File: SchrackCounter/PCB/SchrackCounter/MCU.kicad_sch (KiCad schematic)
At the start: 3 parts, among them U6 ESP32-S3-WROOM-2

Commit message: PCB layout update
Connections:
- net BZ1_PWM: now also U6.12 (IO8)
- net CLK: now also U6.21 (IO13); no longer U6.20 (IO12)
- net GREEN_FLASH: now also U6.23 (IO21)
- net MISO: now also U6.20 (IO12); no longer U6.21 (IO13)
- net MODE: now also U6.39 (IO1)
- net RED_FLASH: now also U6.17 (IO9)
- net RESET: now also U6.35 (IO42)
- net ~{CS1}: now also U6.22 (IO14); no longer U6.17 (IO9)
- net LED_EXT3: now reaches U6.32 (IO39)
- net LED_EXT2: now reaches U6.33 (IO40)
- net LED_EXT1: now reaches U6.34 (IO41)
- net SCHRACK_SW: now reaches U6.38 (IO2)

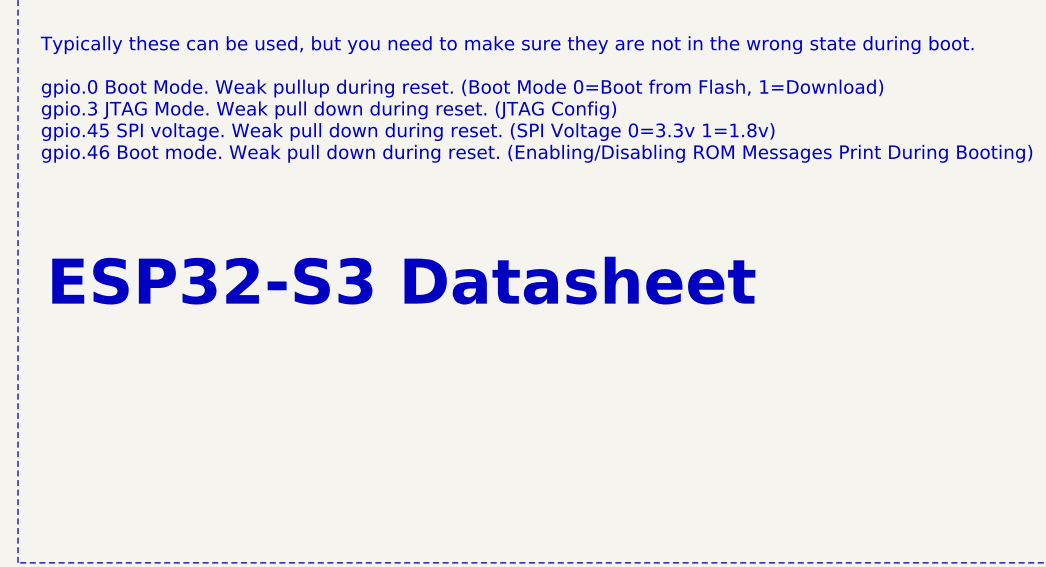
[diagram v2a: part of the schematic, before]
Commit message: PCB update, minor schematic update
PCB routing update, 7segment routing, and minor changes to the 7segments in schematic
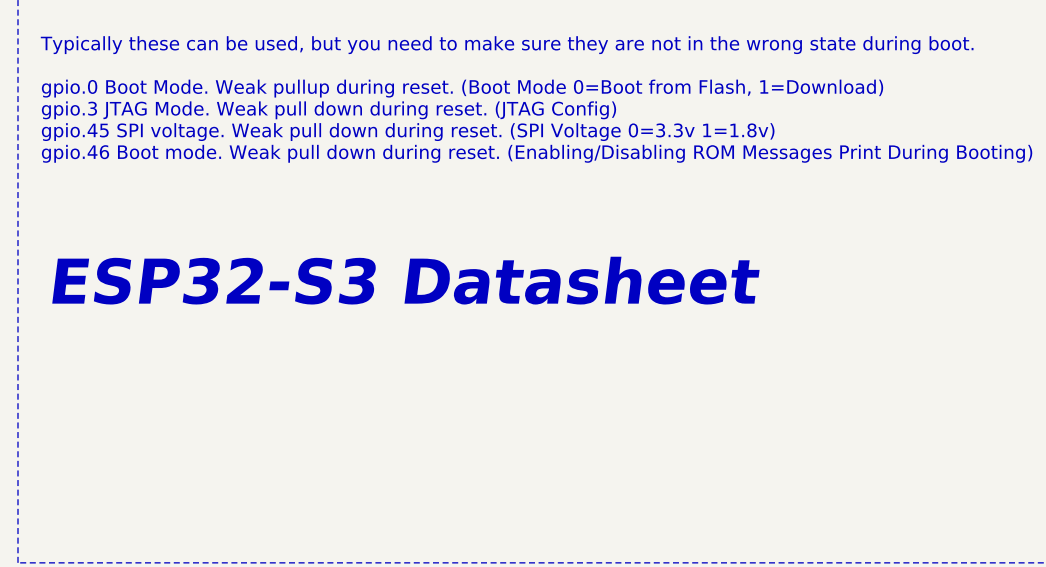
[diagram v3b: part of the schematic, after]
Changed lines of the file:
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@@
 		(effects
 			(font
-				(face "Bahnschrift")
 				(size 5 5)
 				(thickness 1)
 				(bold yes)
-				(color 0 0 0 1)
+				(italic yes)
+				(color 0 0 255 1)
 			)
 			(justify left bottom)

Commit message: SchrackCounter
PCB Finished
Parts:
- C7: value 10uF.mcu -> 10uF
- C8: value 100nF.mcu -> 100nF
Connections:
- net CLK: now also U6.19 (IO11); no longer U6.21 (IO13)
- net GREEN_FLASH: now also U6.17 (IO9); no longer U6.23 (IO21)
- net LED_EXT1: now also U6.32 (IO39); no longer U6.34 (IO41)
- net LED_EXT2: now also U6.31 (IO38); no longer U6.33 (IO40)
- net LED_EXT3: now also U6.23 (IO21); no longer U6.32 (IO39)
- net MISO: now also U6.18 (IO10); no longer U6.20 (IO12)
- net MODE: now also U6.33 (IO40); no longer U6.39 (IO1)
- net MOSI: now also U6.20 (IO12); no longer U6.19 (IO11)
- net RED_FLASH: now also U6.22 (IO14); no longer U6.17 (IO9)
- net SCHRACK_SW: now also U6.34 (IO41); no longer U6.38 (IO2)
- net ~{CS0}: now also U6.4 (IO4); no longer U6.18 (IO10)
- net ~{CS1}: now also U6.21 (IO13); no longer U6.22 (IO14)

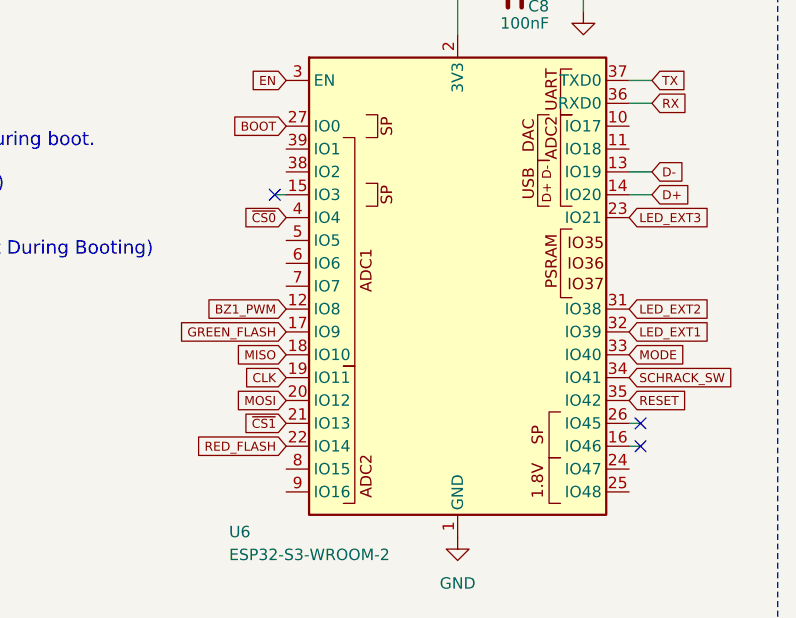
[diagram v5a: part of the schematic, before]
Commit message: PCB LAYOUT UPDATE
Routing, gnd planes
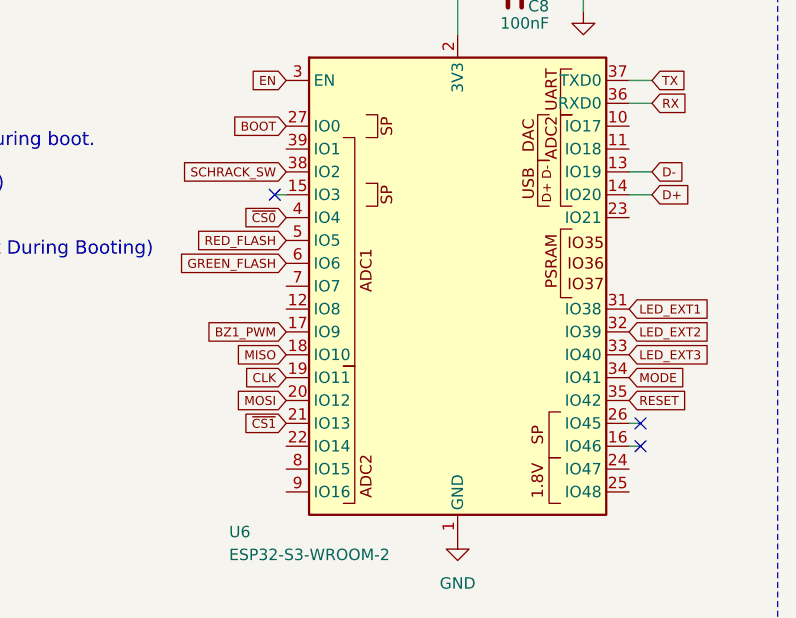
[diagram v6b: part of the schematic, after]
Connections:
- net BZ1_PWM: now also U6.17 (IO9); no longer U6.12 (IO8)
- net GREEN_FLASH: now also U6.6 (IO6); no longer U6.17 (IO9)
- net LED_EXT1: now also U6.31 (IO38); no longer U6.32 (IO39)
- net LED_EXT2: now also U6.32 (IO39); no longer U6.31 (IO38)
- net LED_EXT3: now also U6.33 (IO40); no longer U6.23 (IO21)
- net MODE: now also U6.34 (IO41); no longer U6.33 (IO40)
- net RED_FLASH: now also U6.5 (IO5); no longer U6.22 (IO14)
- net SCHRACK_SW: now also U6.38 (IO2); no longer U6.34 (IO41)

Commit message: PCB finalizing
Final routing and layout
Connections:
- no-connect marks 3 -> 14
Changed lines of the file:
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@@
+	)
+	(no_connect
+		(at 176.53 114.3)
+	)
+	(no_connect
+		(at 176.53 119.38)
+	)
+	(no_connect
+		(at 219.71 119.38)
+	)
+	(no_connect
+		(at 219.71 88.9)
+	)
+	(no_connect
+		(at 219.71 81.28)
+	)
+	(no_connect
+		(at 176.53 81.28)
 	)
 	(no_connect
@@
 		(at 218.44 111.76)
 	)
+	(no_connect
+		(at 219.71 116.84)
+	)
+	(no_connect
+		(at 176.53 116.84)
+	)
+	(no_connect
+		(at 176.53 96.52)
+	)
+	(no_connect
+		(at 219.71 78.74)
+	)
+	(no_connect
+		(at 176.53 99.06)
+	)
 	(wire
 		(pts
@@
 	(wire
 		(pts
+			(xy 217.17 116.84) (xy 219.71 116.84)
+		)
+		(stroke
+			(width 0)
+			(type default)
+		)
+	)
+	(wire
+		(pts
+			(xy 176.53 116.84) (xy 179.07 116.84)
+		)
+		(stroke
+			(width 0)
+			(type default)
+		)
+	)
+	(wire
+		(pts
+			(xy 176.53 99.06) (xy 179.07 99.06)
+		)
+		(stroke
+			(width 0)
+			(type default)
+		)
+	)
+	(wire
+		(pts
 			(xy 219.71 76.2) (xy 217.17 76.2)
 		)
@@
 	(wire
 		(pts
+			(xy 217.17 88.9) (xy 219.71 88.9)
+		)
+		(stroke
+			(width 0)
+			(type default)
+		)
+	)
+	(wire
+		(pts
 			(xy 219.71 86.36) (xy 217.17 86.36)
 		)
@@
 	(wire
 		(pts
+			(xy 176.53 96.52) (xy 179.07 96.52)
+		)
+		(stroke
+			(width 0)
+			(type default)
+		)
+	)
+	(wire
+		(pts
 			(xy 208.28 63.5) (xy 212.09 63.5)
 		)
@@
 	(wire
 		(pts
+			(xy 217.17 78.74) (xy 219.71 78.74)
+		)
+		(stroke
+			(width 0)
+			(type default)
+		)
+	)
+	(wire
+		(pts
 			(xy 212.09 55.88) (xy 212.09 63.5)
 		)
@@
 	(wire
 		(pts
+			(xy 176.53 81.28) (xy 179.07 81.28)
+		)
+		(stroke
+			(width 0)
+			(type default)
+		)
+	)
+	(wire
+		(pts
 			(xy 218.44 111.76) (xy 217.17 111.76)
 		)
@@
 	(wire
 		(pts
+			(xy 176.53 114.3) (xy 179.07 114.3)
+		)
+		(stroke
+			(width 0)
+			(type default)
+		)
+	)
+	(wire
+		(pts
+			(xy 217.17 119.38) (xy 219.71 119.38)
+		)
+		(stroke
+			(width 0)
+			(type default)
+		)
+	)
+	(wire
+		(pts
 			(xy 198.12 55.88) (xy 198.12 63.5)
 		)
@@
 	(wire
 		(pts
+			(xy 217.17 81.28) (xy 219.71 81.28)
+		)
+		(stroke
+			(width 0)
+			(type default)
+		)
+	)
+	(wire
+		(pts
 			(xy 198.12 63.5) (xy 198.12 68.58)
 		)
 		(stroke
+			(width 0)
+			(type default)
+		)
+	)
+	(wire
+		(pts
+			(xy 176.53 119.38) (xy 179.07 119.38)
+		)
+		(stroke

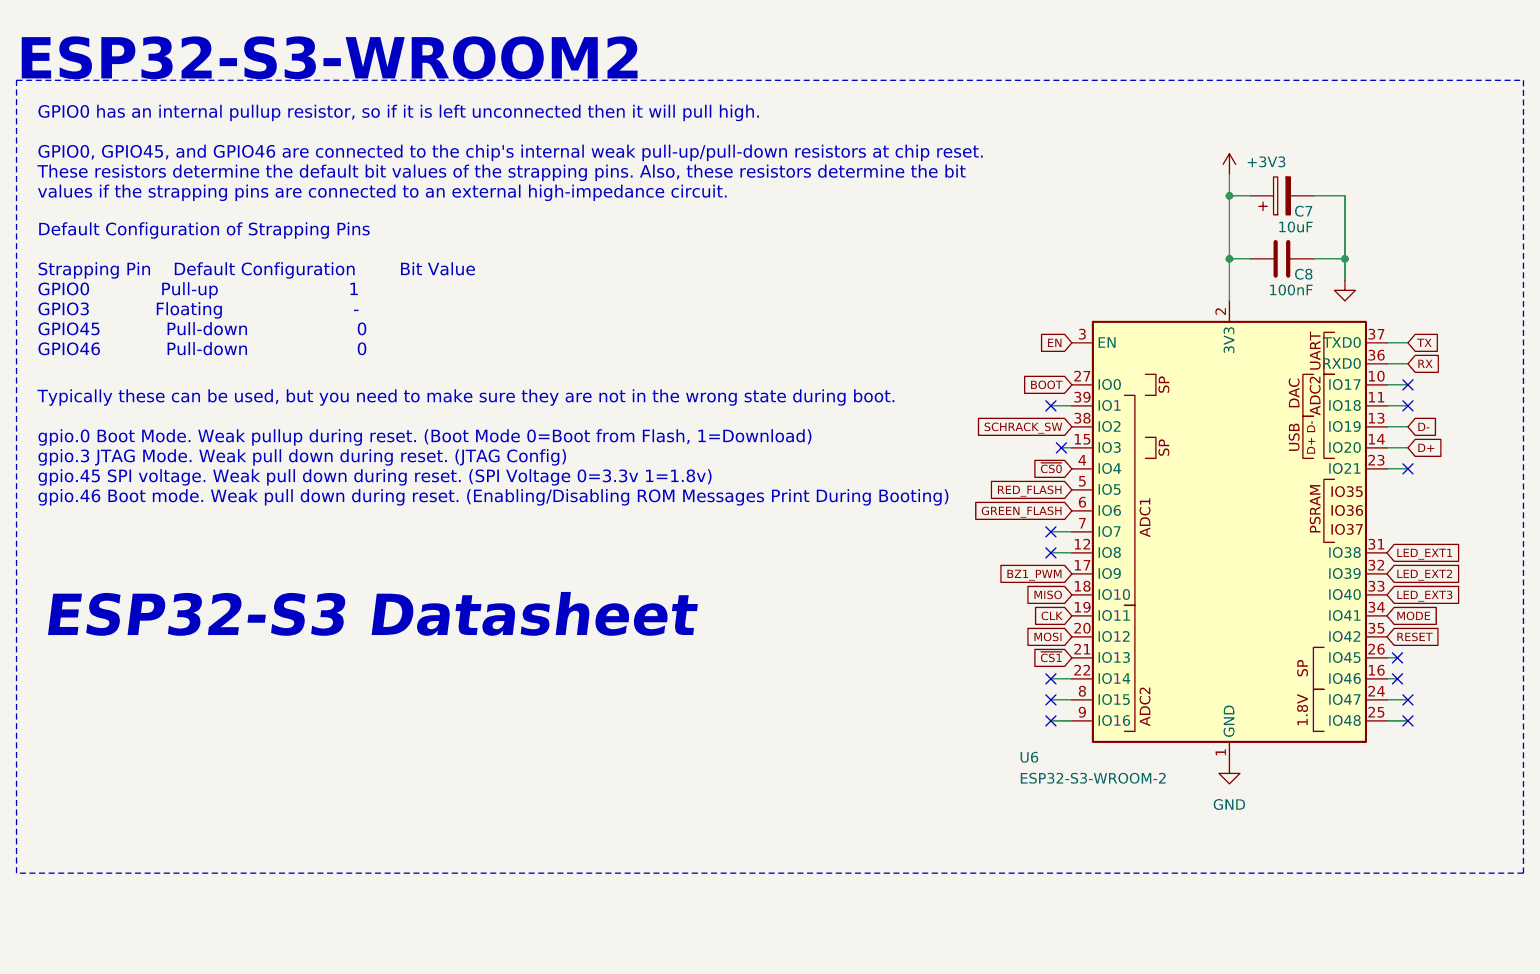
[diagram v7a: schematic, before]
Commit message: Schematic update
Documentation for programming, GPIO pin table :3
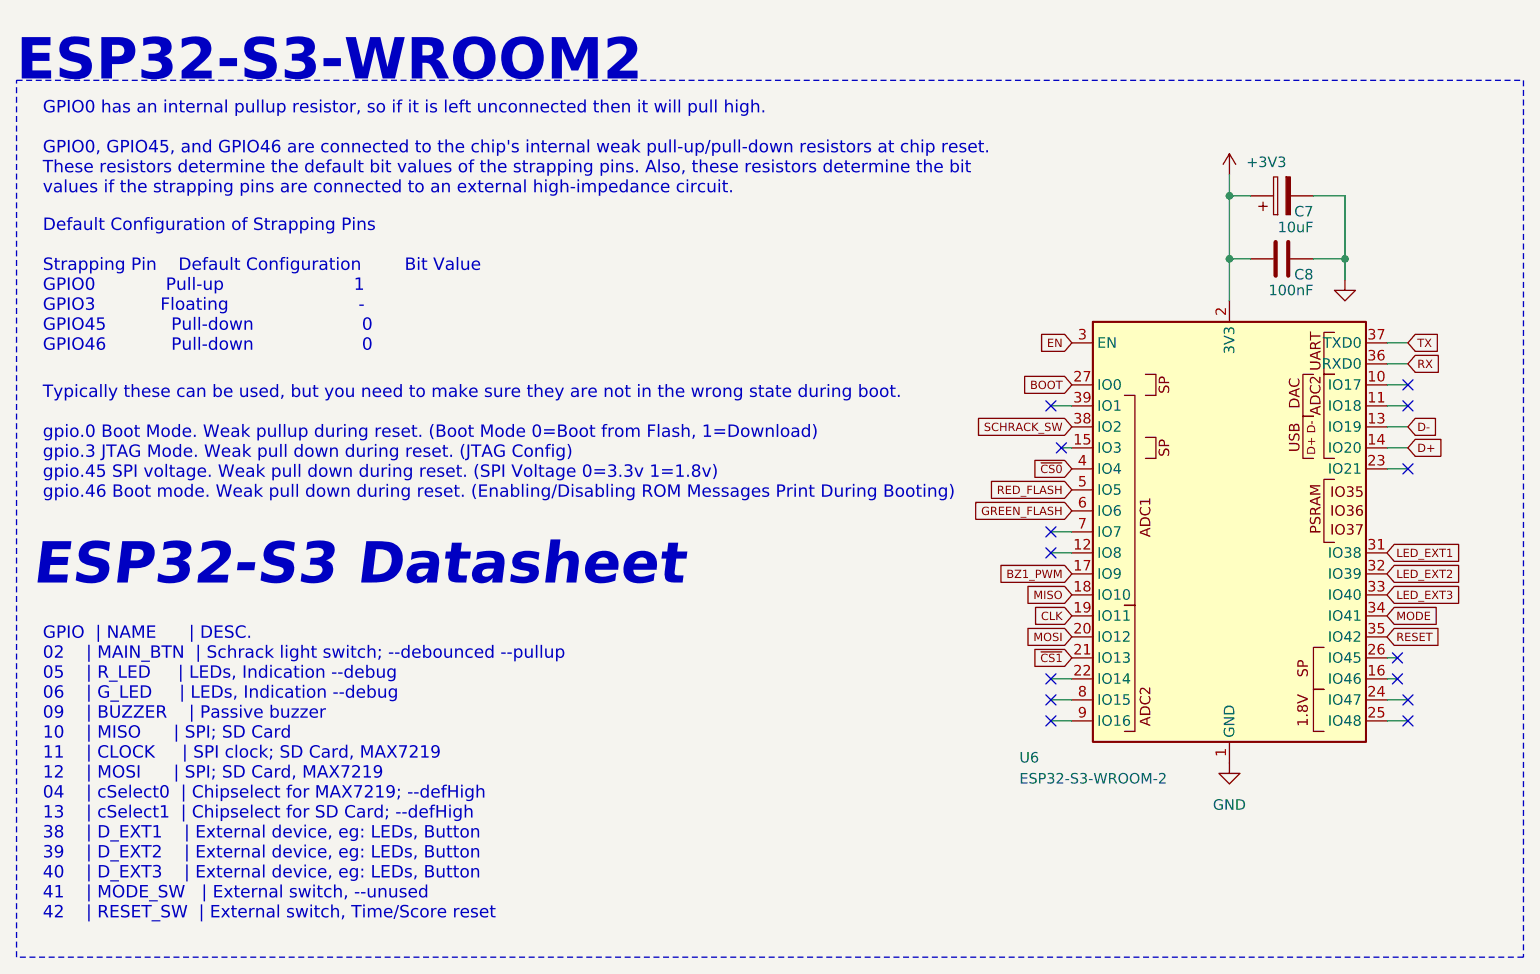
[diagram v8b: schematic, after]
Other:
- note added: "GPIO | NAME | DESC. 02 | MAIN_BTN | Schrack light switch; --debounced --pullup 05 | R_LED | LEDs, Indication --debug 06 | G_LED | LEDs, Indication --debug 09 | BUZZER | Passive buzzer 10 | MISO | SPI; SD Card 11 | CLOCK | SPI clock; SD Card, MAX7219 12 | MOSI | SPI; SD Card, MAX7219 04 | cSelect0 | Chipselect for MAX7219; --defHigh 13 | cSelect1 | Chipselect for SD Card; --defHigh 38 | D_EXT1 | E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"
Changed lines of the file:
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@@
 	(rectangle
 		(start 51.435 41.91)
-		(end 233.68 137.795)
+		(end 233.68 147.955)
 		(stroke
 			(width 0)
@@
 	(text "Default Configuration of Strapping Pins\n\nStrapping Pin	Default Configuration		Bit Value\nGPIO0 			Pull-up						1\nGPIO3			Floating						-\nGPIO45			Pull-down					0\nGPIO46			Pull-down					0"
 		(exclude_from_sim no)
-		(at 53.975 75.565 0)
+		(at 54.61 74.93 0)
 		(effects
 			(font
@@
 			)
 			(justify left bottom)
+		)
+	)
+	(text "GPIO  | NAME      | DESC. \n02    | MAIN_BTN  | Schrack light switch; --debounced --pullup \n05    | R_LED     | LEDs, Indication --debug\n06    | G_LED     | LEDs, Indication --debug\n09    | BUZZER    | Passive buzzer\n10    | MISO      | SPI; SD Card\n11    | CLOCK     | SPI clock; SD Card, MAX7219\n12    | MOSI      | SPI; SD Card, MAX7219\n04    | cSelect0  | Chipselect for MAX7219; --defHigh\n13    | cSelect1  | Chipselect for SD Card; --defHigh\n38    | D_EXT1    | External device, eg: LEDs, Button\n39    | D_EXT2    | External device, eg: LEDs, Button\n40    | D_EXT3    | External device, eg: LEDs, Button\n41    | MODE_SW   | External switch, --unused\n42    | RESET_SW  | External switch, Time/Score reset\n\n"
+		(exclude_from_sim no)
+		(at 54.61 127 0)
+		(effects
+			(font
+				(face "Consolas")
+				(size 1.5 1.5)
+				(color 0 0 0 1)
+			)
+			(justify left)
 		)
 	)
@@
 	(text "GPIO0 has an internal pullup resistor, so if it is left unconnected then it will pull high.\n\nGPIO0, GPIO45, and GPIO46 are connected to the chip's internal weak pull-up/pull-down resistors at chip reset.\nThese resistors determine the default bit values of the strapping pins. Also, these resistors determine the bit\nvalues if the strapping pins are connected to an external high-impedance circuit."
 		(exclude_from_sim no)
-		(at 53.975 56.515 0)
+		(at 54.61 55.88 0)
 		(effects
 			(font
@@
 	(text "Typically these can be used, but you need to make sure they are not in the wrong state during boot.\n\ngpio.0 Boot Mode. Weak pullup during reset. (Boot Mode 0=Boot from Flash, 1=Download)\ngpio.3 JTAG Mode. Weak pull down during reset. (JTAG Config)\ngpio.45 SPI voltage. Weak pull down during reset. (SPI Voltage 0=3.3v 1=1.8v)\ngpio.46 Boot mode. Weak pull down during reset. (Enabling/Disabling ROM Messages Print During Booting)"
 		(exclude_from_sim no)
-		(at 53.975 93.345 0)
+		(at 54.61 92.71 0)
 		(effects
 			(font
@@
 	(text "ESP32-S3 Datasheet"
 		(exclude_from_sim no)
-		(at 54.61 109.855 0)
+		(at 53.34 103.505 0)
 		(effects
 			(font
